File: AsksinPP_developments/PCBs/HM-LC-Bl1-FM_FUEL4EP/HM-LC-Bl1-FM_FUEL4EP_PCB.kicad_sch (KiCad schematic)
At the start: 69 parts, among them J1 Down Button, J10 charge, J11 24V PSU, J12 230V Netzteil Relais, J13 Velux Motor, J14 Motor direction LEDs, J15 Charge Indication LED, J16 H Brücke Relais In, J17 Motor Relais In, J18 Conn_01x03, J19 GND, J2 Up Button, J3 Dual LED, J4 Config Button, J5 ISP Programmer, J6 Accumulator, J7 LED rot, J8 LED grün, J9 LED gelb, Q1 IRLU024N, Q2 BD238, Q3 IRF9Z34N, Q4 2N7000, Q5 MCP1702-2802E_TO

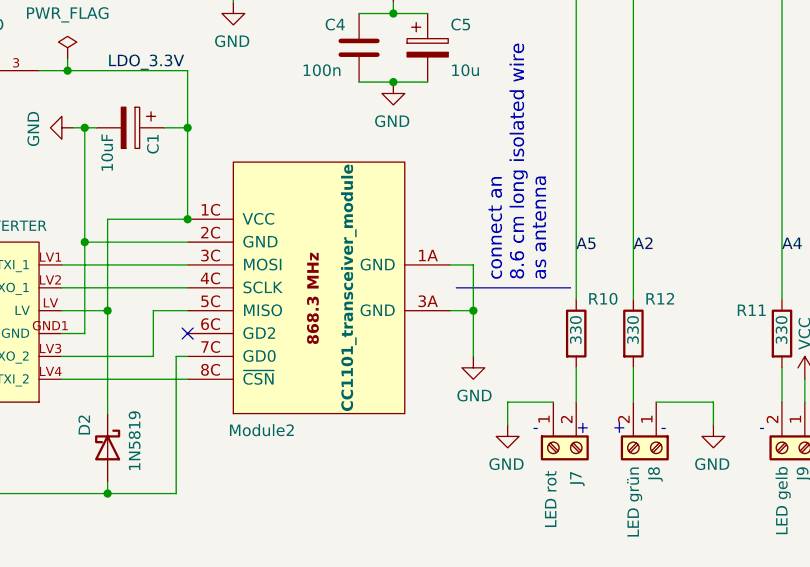
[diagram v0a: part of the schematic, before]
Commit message: PCBs: KiCAD6 required improvements of layout data bases; added E07-900M10S into FUEL and footprint library
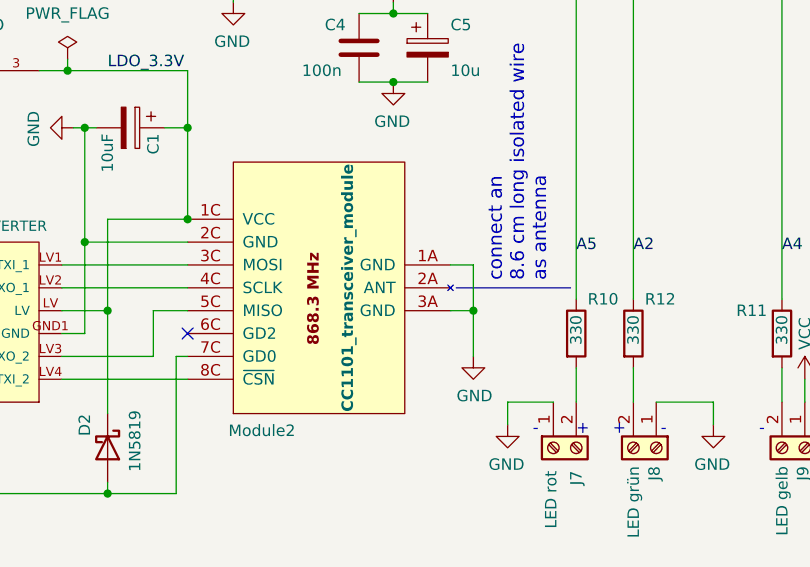
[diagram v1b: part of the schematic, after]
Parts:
- Q5: footprint FUEL4EP:TO127P254X533-3 -> TO127P254X533-3
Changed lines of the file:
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@@
     (property "Reference" "Q5" (id 0) (at 40.64 151.13 0))
     (property "Value" "MCP1702-2802E_TO" (id 1) (at 46.99 139.7 0))
-    (property "Footprint" "FUEL4EP:TO127P254X533-3" (id 2) (at 52.07 139.7 0)
+    (property "Footprint" "TO127P254X533-3" (id 2) (at 52.07 139.7 0)
       (effects (font (size 1.27 1.27)) (justify left bottom) hide)
     )
@@
     )
     (path "/00000000-0000-0000-0000-0000619a7cde"
-      (reference "Q5") (unit 1) (value "MCP1702-2802E_TO") (footprint "FUEL4EP:TO127P254X533-3")
+      (reference "Q5") (unit 1) (value "MCP1702-2802E_TO") (footprint "TO127P254X533-3")
     )
     (path "/00000000-0000-0000-0000-00005abe25c7"

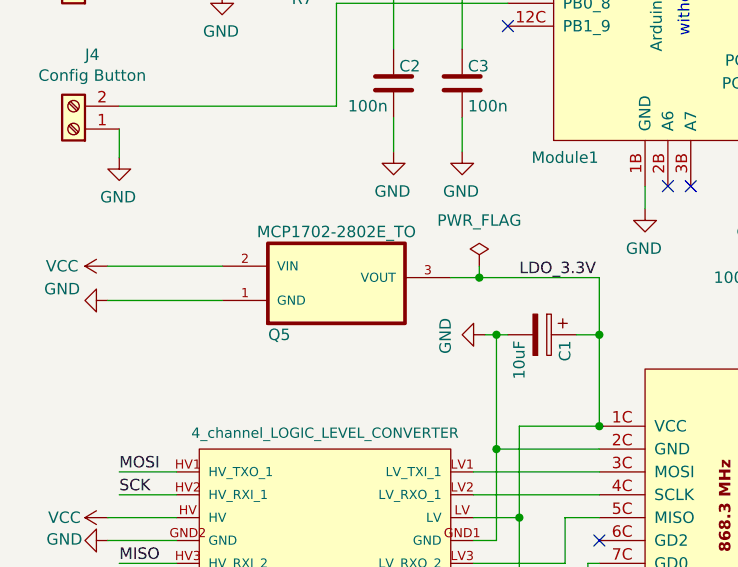
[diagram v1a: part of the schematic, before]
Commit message: HM-LC-Bl1-FM_FUEL4EP and HB-UNI-SenAct-4-4-SC_DS_FUEL4EP: fix of MCP1702 from 2.8V to 3.3V version
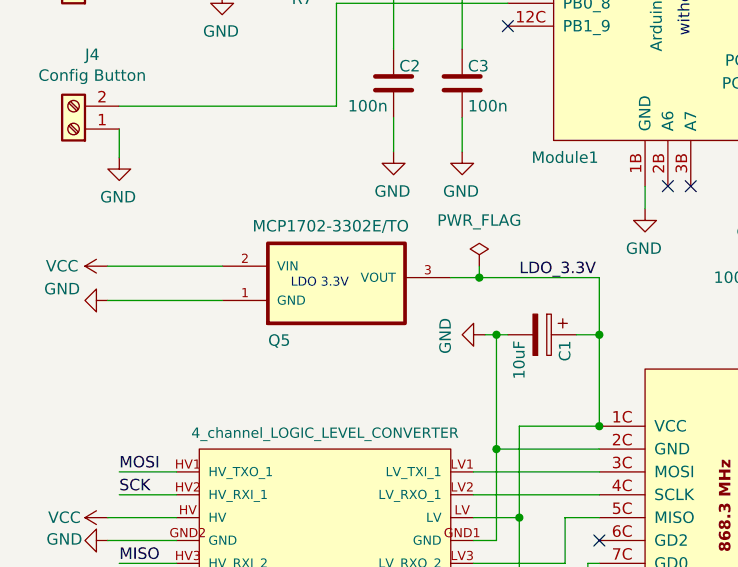
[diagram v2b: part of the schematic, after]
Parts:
- removed Q5: MCP1702-2802E_TO, TO127P254X533-3, symbol FUEL4EP:MCP1702-2802E_TO
- added Q5: MCP1702-3302E/TO, TO127P254X533-3, symbol FUEL4EP:MCP1702-3302E/TO
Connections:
- net GND: now also Q5.1 (GND)
- net LDO_3.3V: now also Q5.3 (VOUT)
- net VCC: now also Q5.2 (VIN)
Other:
- note added: "LDO 3.3V"
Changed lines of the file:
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@@
   (title_block
     (title "HM-LC-Bl1-FM_DG")
-    (date "2023-07-14")
-    (rev "1.2")
+    (date "2023-07-28")
+    (rev "1.3")
     (company "FUEL4EP")
     (comment 1 "24V Polwendeaktor für VELUX Rolladen AsksinPP PCB")
@@
     (effects (font (size 1.27 1.27)) (justify left bottom))
   )
+  (text "LDO 3.3V" (at 41.91 146.05 0)
+    (effects (font (size 1 1)) (justify left bottom))
+  )
   (text "-\n" (at 114.554 185.42 0)
     (effects (font (size 1.27 1.27)) (justify left bottom))
@@
     (pin "1")
   )
-  (symbol (lib_id "FUEL4EP:MCP1702-2802E_TO") (at 39.37 140.97 0) (unit 1)
-    (in_bom yes) (on_board yes)
-    (property "Reference" "Q5" (id 0) (at 40.64 151.13 0))
-    (property "Value" "MCP1702-2802E_TO" (id 1) (at 46.99 139.7 0))
-    (property "Footprint" "TO127P254X533-3" (id 2) (at 52.07 139.7 0)
-      (effects (font (size 1.27 1.27)) (justify left bottom) hide)
-    )
-    (property "Datasheet" "" (id 3) (at 52.07 139.7 0)
-      (effects (font (size 1.27 1.27)) (justify left bottom) hide)
-    )
-    (property "OC_FARNELL" "1331485" (id 4) (at 52.07 139.7 0)
-      (effects (font (size 1.27 1.27)) (justify left bottom) hide)
-    )
-    (property "SUPPLIER" "Microchip" (id 5) (at 52.07 139.7 0)
-      (effects (font (size 1.27 1.27)) (justify left bottom) hide)
-    )
-    (property "MPN" "MCP1702-2802E/TO" (id 6) (at 52.07 139.7 0)
-      (effects (font (size 1.27 1.27)) (justify left bottom) hide)
-    )
-    (property "PACKAGE" "TO-92" (id 7) (at 52.07 139.7 0)
-      (effects (font (size 1.27 1.27)) (justify left bottom) hide)
-    )
-    (property "OC_NEWARK" "34M7419" (id 8) (at 52.07 139.7 0)
-      (effects (font (size 1.27 1.27)) (justify left bottom) hide)
-    )
-    (pin "1")
-    (pin "2")
-    (pin "3")
-  )
   (symbol (lib_id "power:VCC") (at 144.78 179.07 0) (unit 1)
     (in_bom yes) (on_board yes)
@@
     (pin "1")
   )
+  (symbol (lib_id "FUEL4EP:MCP1702-3302E{slash}TO") (at 39.37 140.97 0) (unit 1)
+    (in_bom yes) (on_board yes)
+    (property "Reference" "Q5" (id 0) (at 40.64 151.765 0))
+    (property "Value" "MCP1702-3302E/TO" (id 1) (at 46.355 139.065 0))
+    (property "Footprint" "TO127P254X533-3" (id 2) (at 45.72 135.255 0)
+      (effects (font (size 1.27 1.27)) (justify left bottom) hide)
+    )
+    (property "Datasheet" "https://ww1.microchip.com/downloads/en/DeviceDoc/22008E.pdf" (id 3) (at 45.72 140.335 0)
+      (effects (font (size 1.27 1.27)) (justify left bottom) hide)
+    )
+    (property "SUPPLIER" "Microchip" (id 4) (at 45.72 137.795 0)
+      (effects (font (size 1.27 1.27)) (justify left bottom) hide)
+    )
+    (property "PACKAGE" "TO-92" (id 5) (at 45.72 132.715 0)
+      (effects (font (size 1.27 1.27)) (justify left bottom) hide)
+    )
+    (pin "1")
+    (pin "2")
+    (pin "3")
+  )
   (sheet_instances
     (path "/" (page "1"))
@@
       (reference "Q4") (unit 1) (value "2N7000") (footprint "Package_TO_SOT_THT:TO-92_Inline")
     )
-    (path "/00000000-0000-0000-0000-0000619a7cde"
-      (reference "Q5") (unit 1) (value "MCP1702-2802E_TO") (footprint "TO127P254X533-3")
+    (path "/c16c85c1-815e-4577-8ce3-b2d2c45e0af1"
+      (reference "Q5") (unit 1) (value "MCP1702-3302E/TO") (footprint "TO127P254X533-3")
     )
     (path "/00000000-0000-0000-0000-00005abe25c7"

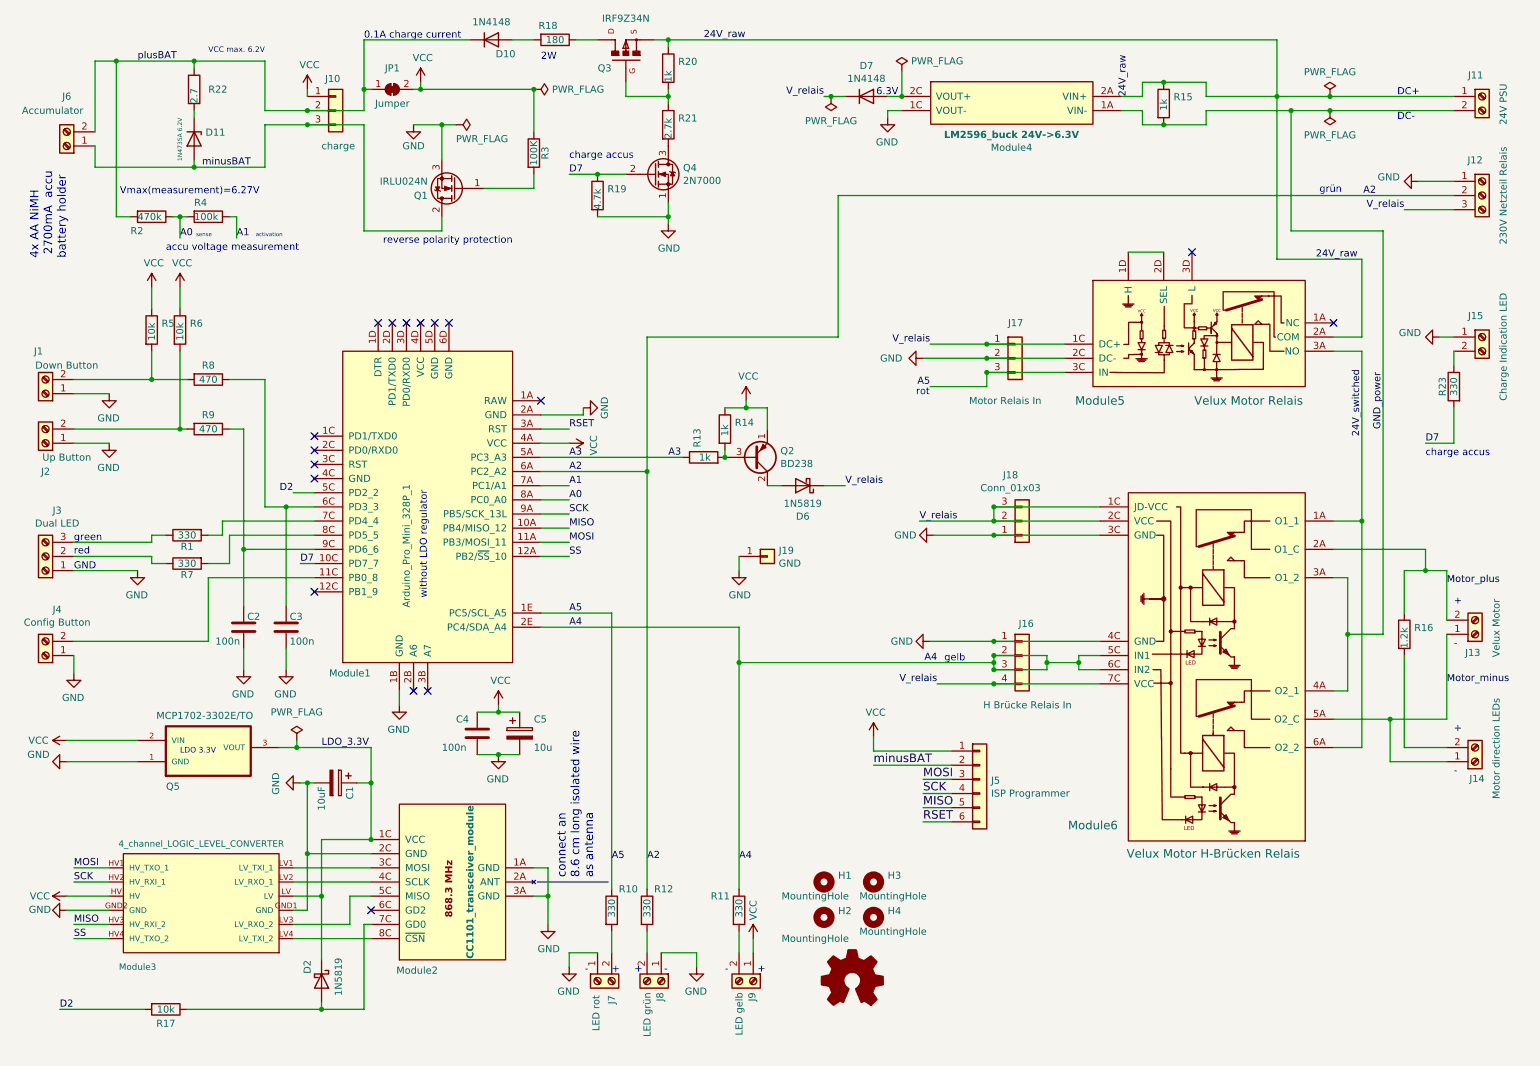
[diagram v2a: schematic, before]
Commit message: PCBs/HM-LC-Bl1-FM_FUEL4EP: migration to KiCAD 8
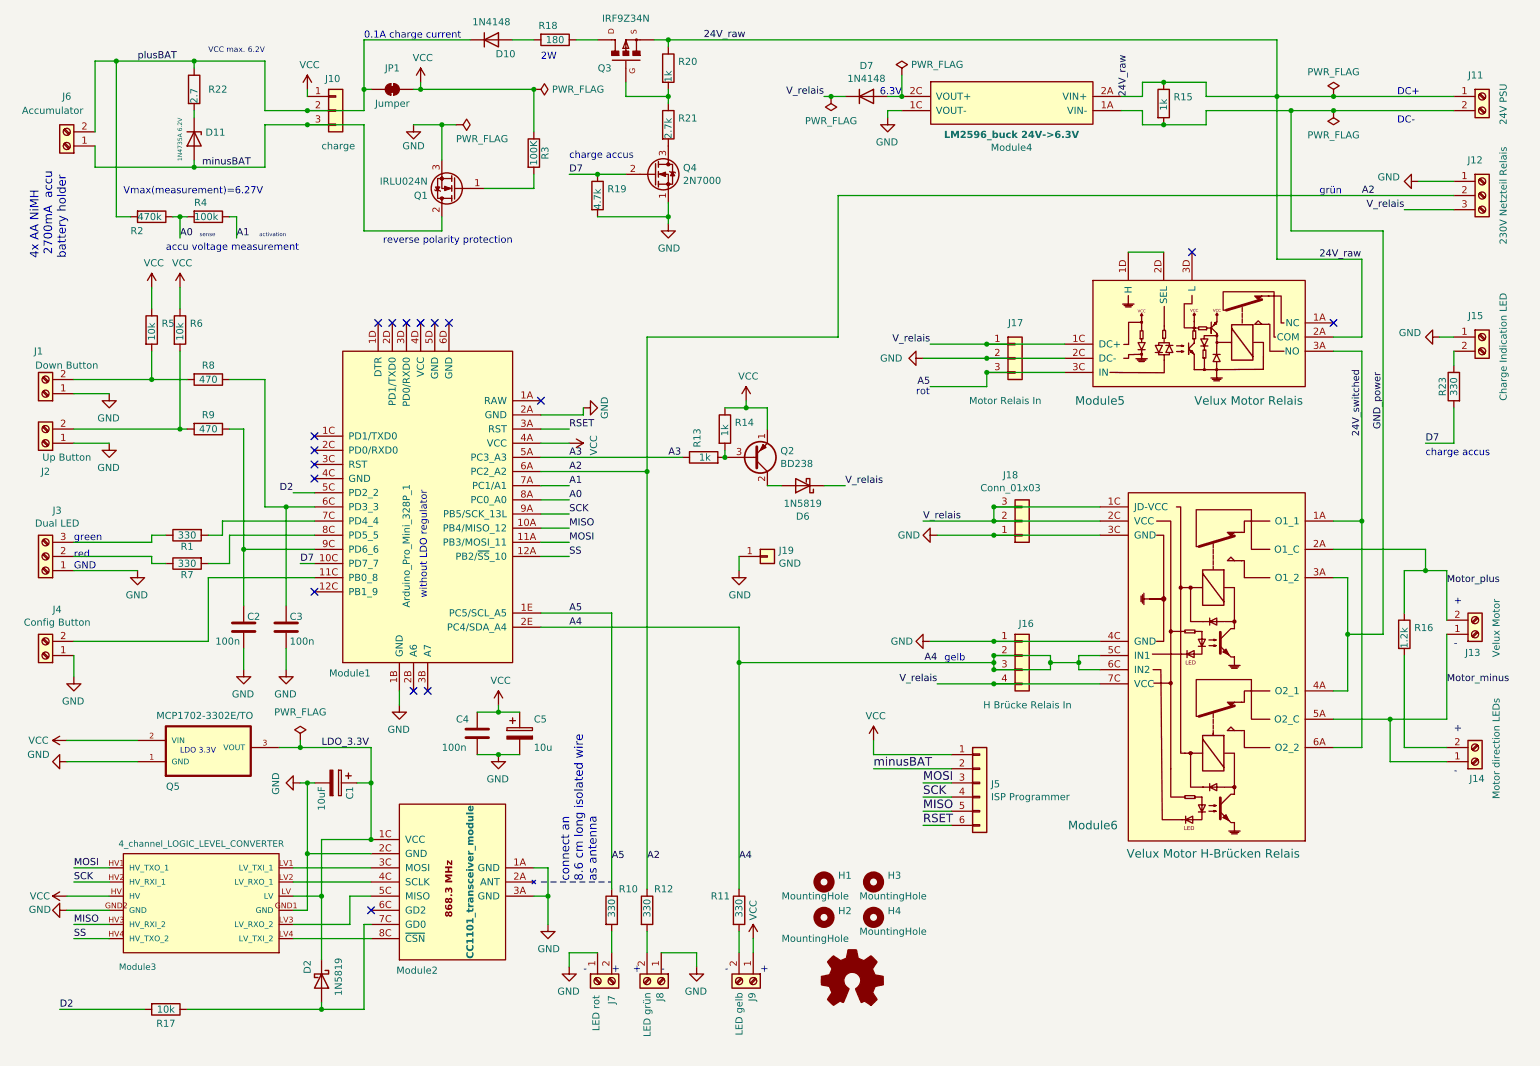
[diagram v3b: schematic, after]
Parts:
- Q5: footprint TO127P254X533-3 -> FUEL4EP:TO127P254X533-3; symbol FUEL4EP:MCP1702-3302E/TO -> FUEL4EP:MCP1702-3302E/TO
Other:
- moved on the sheet: J5
